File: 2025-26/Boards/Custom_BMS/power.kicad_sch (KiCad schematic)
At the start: 0 parts

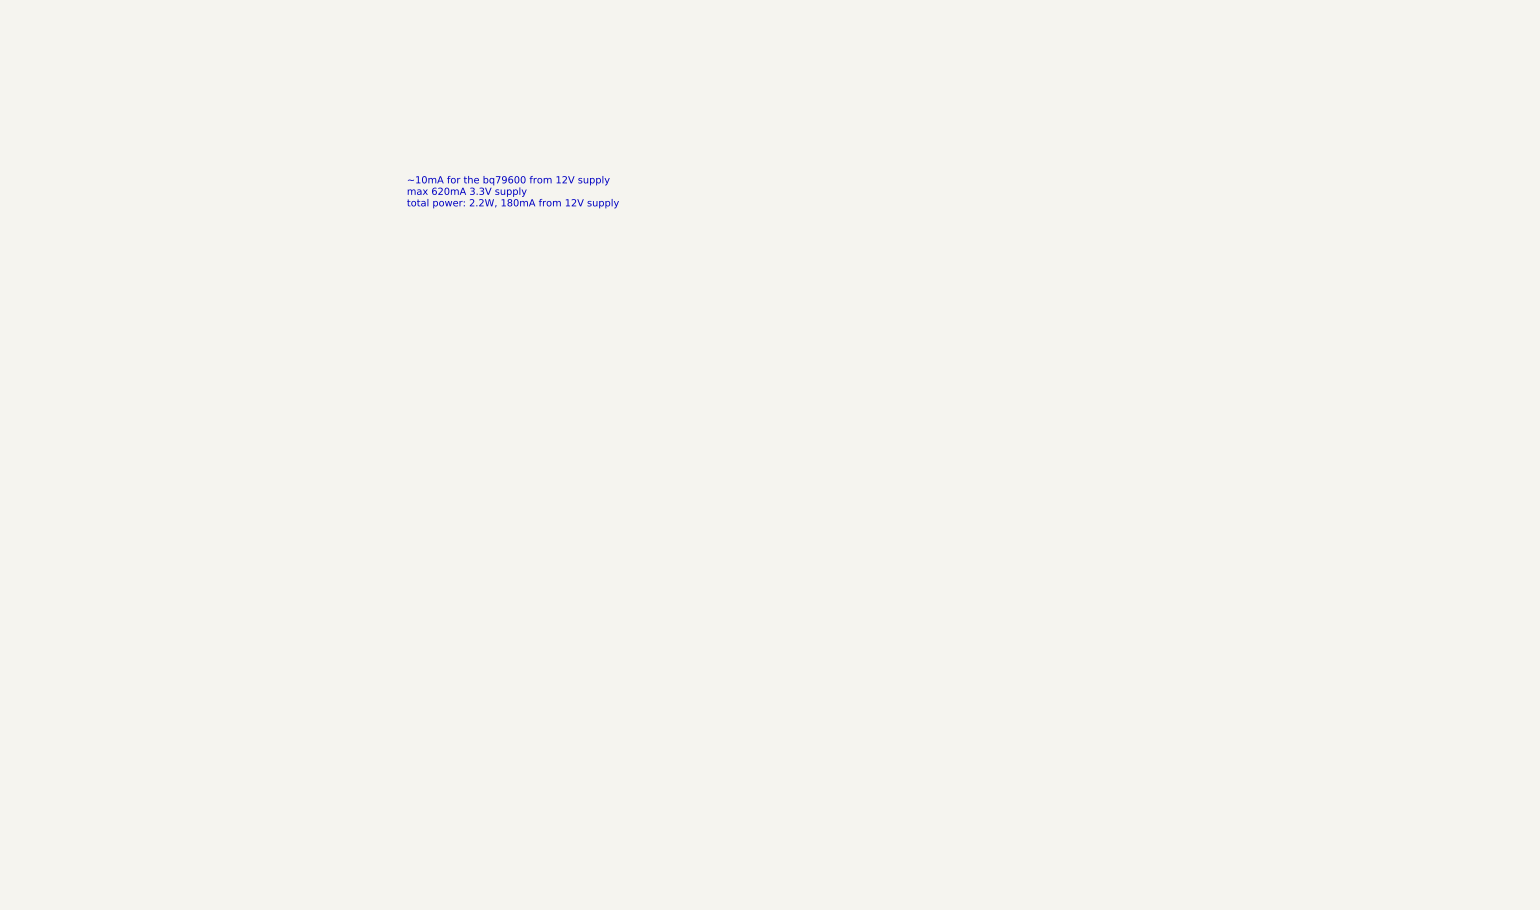
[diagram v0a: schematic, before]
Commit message: designed power circuitry
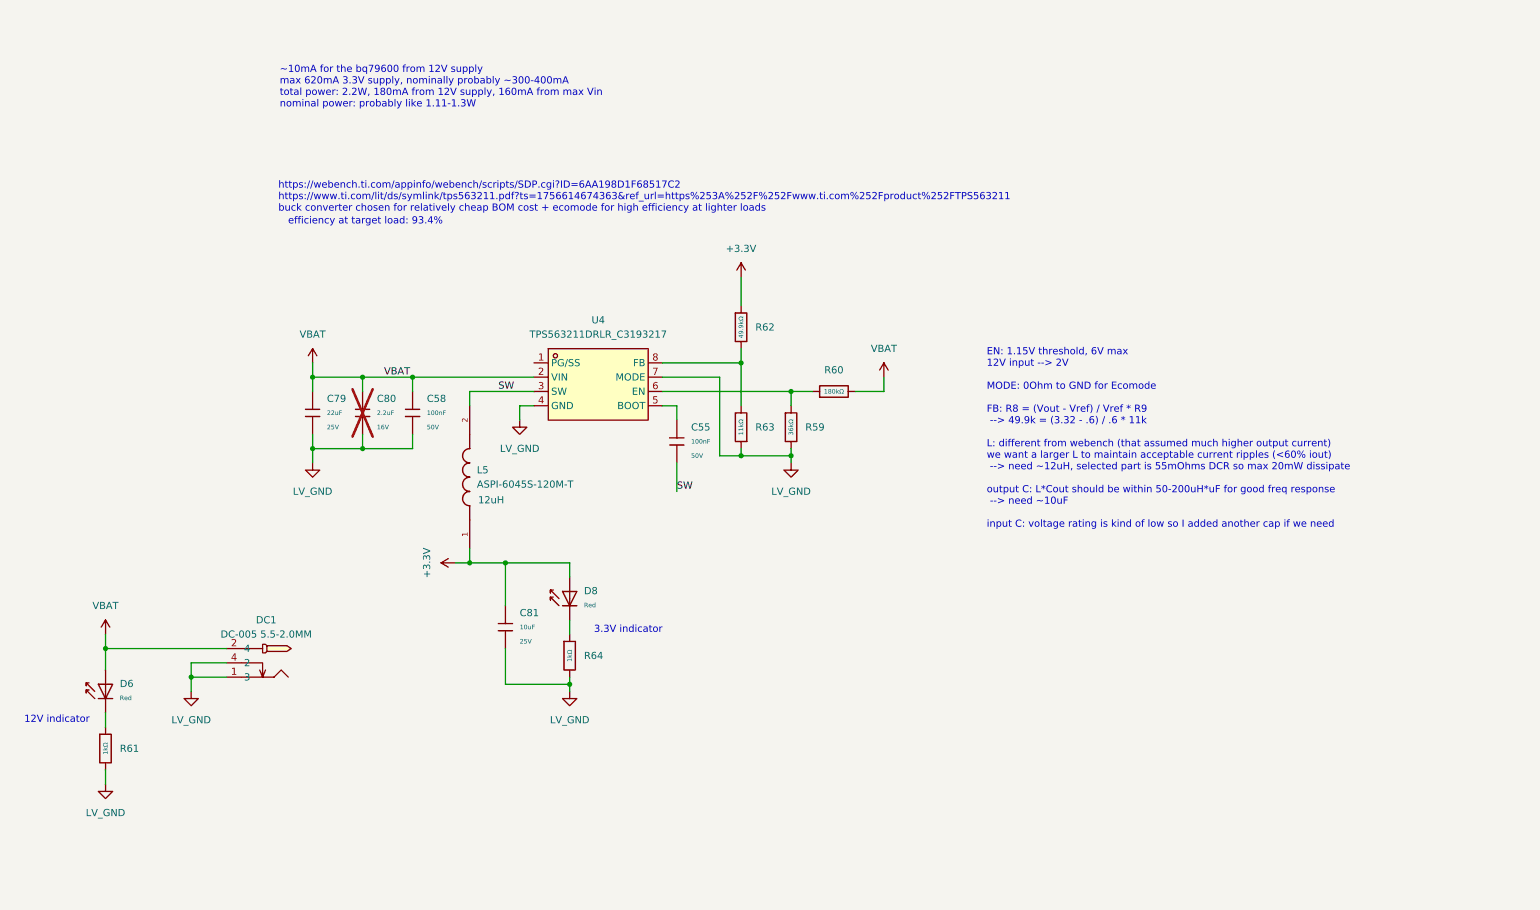
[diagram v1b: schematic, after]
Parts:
- added C55, C58: 100nF, PCM_JLCPCB:C_0603, symbol PCM_JLCPCB-Capacitors:0603,100nF
- added C79: 22uF, PCM_JLCPCB:C_0805, symbol PCM_JLCPCB-Capacitors:0805,22uF
- added C80: 2.2uF, PCM_JLCPCB:C_0603, symbol PCM_JLCPCB-Capacitors:0603,2.2uF
- added C81: 10uF, PCM_JLCPCB:C_0805, symbol PCM_JLCPCB-Capacitors:0805,10uF
- added D6, D8: Red, PCM_JLCPCB:D_0603, symbol PCM_JLCPCB-Diodes:LED,0603,Red
- added DC1: DC-005 5.5-2.0MM, easyeda2kicad:DC-IN-TH_DC-005-5.5-2.0, symbol easyeda2kicad:DC-0055.5-2.0MM
- added L5: ASPI-6045S-120M-T, ASPI-6045S-120M-T:IND_ASPI-6045S-120M-T, symbol ASPI-6045S-120M-T:ASPI-6045S-120M-T
- added R59: 36kΩ, PCM_JLCPCB:R_0603, symbol PCM_JLCPCB-Resistors:0603,36kΩ
- added R60: 180kΩ, PCM_JLCPCB:R_0603, symbol PCM_JLCPCB-Resistors:0603,180kΩ
- added R61, R64: 1kΩ, PCM_JLCPCB:R_0603, symbol PCM_JLCPCB-Resistors:0603,1kΩ
- added R62: 49.9kΩ, PCM_JLCPCB:R_0603, symbol PCM_JLCPCB-Resistors:0603,49.9kΩ
- added R63: 11kΩ, PCM_JLCPCB:R_0603, symbol PCM_JLCPCB-Resistors:0603,11kΩ
- added U4: TPS563211DRLR_C3193217, easyeda2kicad:SOT-583-8_L2.1-W1.6-P0.50-LS1.6-BL, symbol easyeda2kicad:TPS563211DRLR_C3193217
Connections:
- new net: D8.1, R64.1
- new net: C55.1, U4.5 (BOOT)
- new net: D6.1, R61.1
- new net: R59.1, R60.1, U4.6 (EN)
- new net: R62.2, R63.2, U4.8 (FB)
- new net +3.3V: C81.1, D8.2, L5.1, R62.1
- new net LV_GND: C58.2, C79.2, C80.2, C81.2, DC1.1 (3), DC1.4 (2), R59.2, R61.2, R63.1, R64.2, U4.4 (GND), U4.7 (MODE)
- new net SW: C55.2, L5.2, U4.3 (SW)
- new net VBAT: C58.1, C79.1, C80.1, D6.2, DC1.2 (4), R60.2, U4.2 (VIN)
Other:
- note added: "12V indicator"
- note added: "3.3V indicator"
- note added: "EN: 1.15V threshold, 6V maxr 12V input --> 2V MODE: 0Ohm to GND for Ecomode FB: R8 = (Vout - Vref) / Vref * R9 --> 49.9k = (3.32 - .6) / .6 * 11k L: different from webench (that assumed much higher output current) we want a larger L to maintain acceptable current ripples (<60% iout) --> need ~12uH, selected part is 55mOhms DCR so max 20mW dissipate output C: L*Cout should be within 50-200uH*uF fo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"
- note added: "efficiency at target load: 93.4%"
- note added: "https://webench.ti.com/appinfo/webench/scripts/SDP.cgi?ID=6AA198D1F68517C2 https://www.ti.com/lit/ds/symlink/tps563211.pdf?ts=1756614674363&ref_url=https%253A%252F%252Fwww.ti.com%252Fproduct%252FTPS563211 buck converter chosen for relatively cheap BOM cost + ecomode for high efficiency at lighter loads"
- note added: "~10mA for the bq79600 from 12V supply max 620mA 3.3V supply, nominally probably ~300-400mA total power: 2.2W, 180mA from 12V supply, 160mA from max Vin nominal power: probably like 1.11-1.3W"
- note removed: "~10mA for the bq79600 from 12V supply max 620mA 3.3V supply total power: 2.2W, 180mA from 12V supply"

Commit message: reviewed and modified power
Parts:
- removed C81: 10uF, PCM_JLCPCB:C_0805, symbol PCM_JLCPCB-Capacitors:0805,10uF
- removed L5: ASPI-6045S-120M-T, ASPI-6045S-120M-T:IND_ASPI-6045S-120M-T, symbol ASPI-6045S-120M-T:ASPI-6045S-120M-T
- added C10: 4.7uF, PCM_JLCPCB:C_0603, symbol PCM_JLCPCB-Capacitors:0603,4.7uF
- added C9: 10uF, PCM_JLCPCB:C_0603, symbol PCM_JLCPCB-Capacitors:0603,10uF,(2)
- added L5: SRR1206-120ML, IND_BOURNS_SRR1240, symbol SRR1206-120ML:SRR1206-120ML
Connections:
- net +3.3V: now also C10.1, C9.1, L5.2
- net LV_GND: now also C10.2, C9.2
- net SW: now also L5.1
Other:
- note added: "efficiency at target load: 92% thermals: 3.3*~.5*.08*70C/W = ~8C rise"
- note added: "slight correction to the above justification- current ripple is not the best way to calculate it since the buck converter automatically switches to DCM. We still care about voltage ripple though. Below is the current ripple calculation based on voltage ripple, and subsequent inductance. Based on 10mV Vripple and 22uF cap. However, I did not use 22uF (went smaller) since the LC product goes a litt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"
- note removed: "efficiency at target load: 93.4%"
- moved on the sheet: C55, C58, C79, C80, D6, D8, DC1, R59, R60, R61, R62, R63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

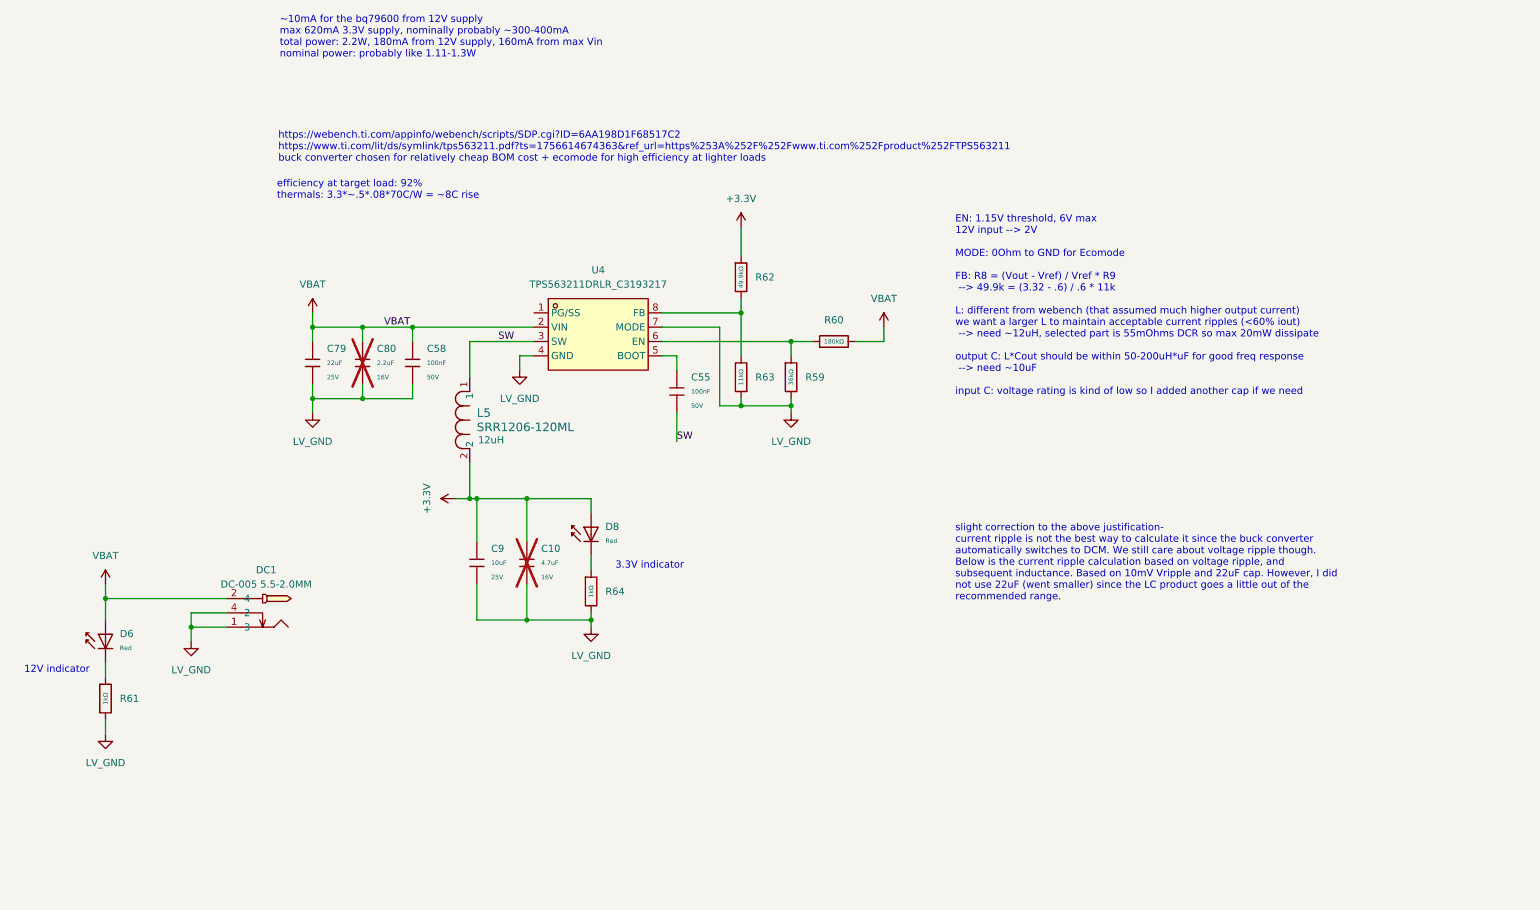
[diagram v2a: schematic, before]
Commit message: added CAN, UART
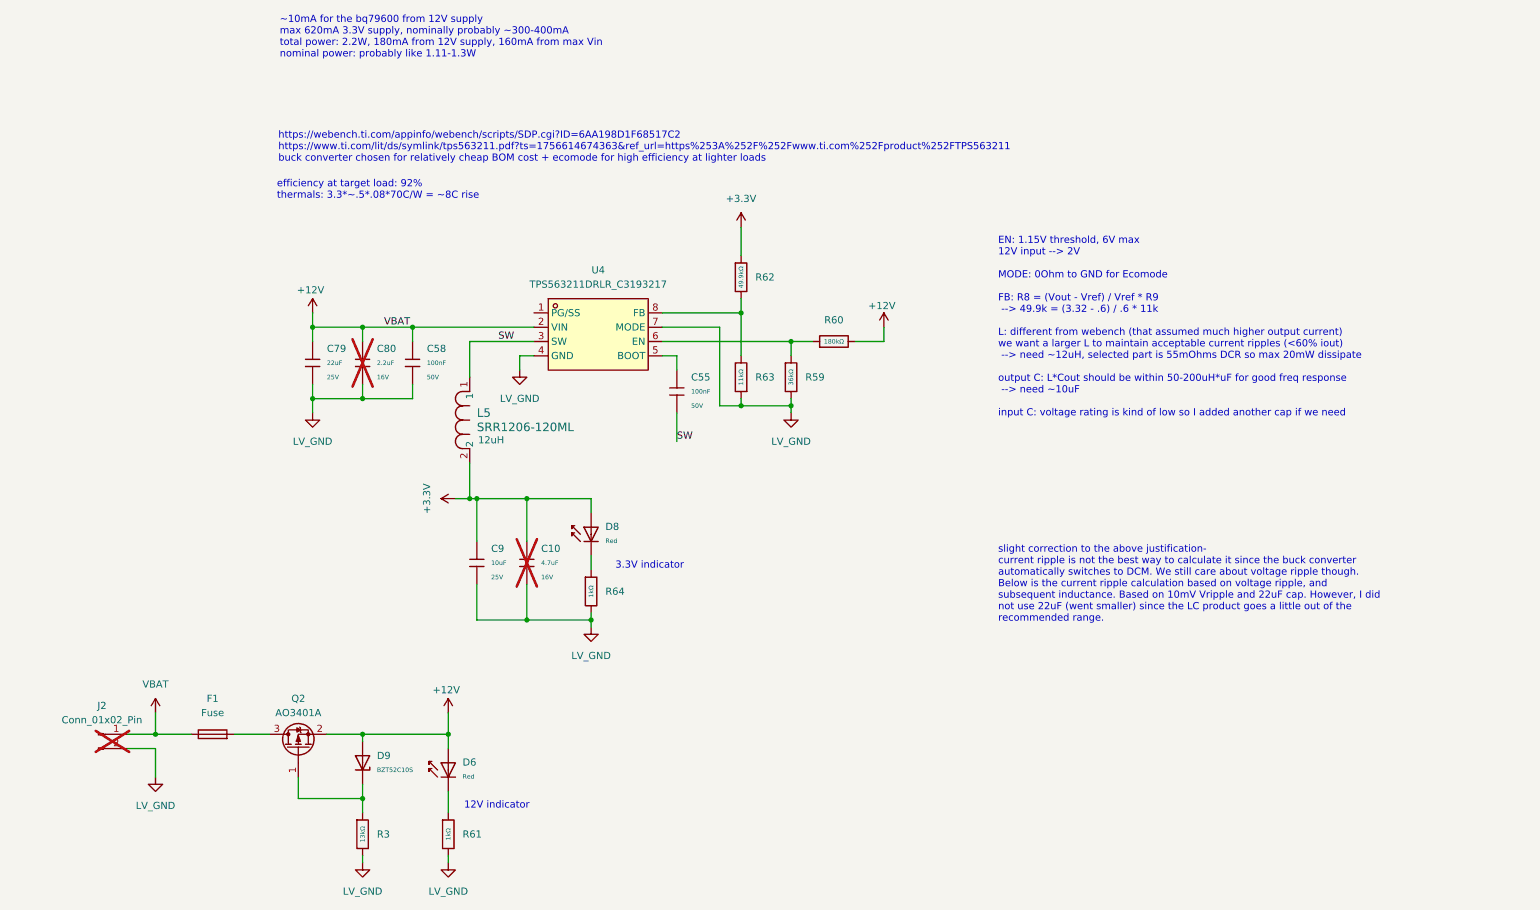
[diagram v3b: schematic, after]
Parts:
- removed DC1: DC-005 5.5-2.0MM, easyeda2kicad:DC-IN-TH_DC-005-5.5-2.0, symbol easyeda2kicad:DC-0055.5-2.0MM
- added D9: BZT52C10S, PCM_JLCPCB:D_SOD-323, symbol PCM_JLCPCB-Diodes:Zener,BZT52C10S
- added F1: Fuse, symbol Device:Fuse
- added J2: Conn_01x02_Pin, symbol Connector:Conn_01x02_Pin
- added Q2: AO3401A, Package_TO_SOT_SMD:SOT-23, symbol Transistor_FET:AO3401A
- added R3: 13kΩ, PCM_JLCPCB:R_0603, symbol PCM_JLCPCB-Resistors:0603,13kΩ
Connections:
- net LV_GND: now also J2.2 (Pin_2), R3.2
- net VBAT renamed +12V
- net +12V: now also D9.2, F1.1, J2.1 (Pin_1), Q2.2 (S)
- new net: D9.1, Q2.1 (G), R3.1
- new net: F1.2, Q2.3 (D)
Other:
- moved on the sheet: D6, R61

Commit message: started layout
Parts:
- removed C10: 4.7uF, PCM_JLCPCB:C_0603, symbol PCM_JLCPCB-Capacitors:0603,4.7uF
- removed C55: 100nF, PCM_JLCPCB:C_0603, symbol PCM_JLCPCB-Capacitors:0603,100nF
- removed C79: 22uF, PCM_JLCPCB:C_0805, symbol PCM_JLCPCB-Capacitors:0805,22uF
- removed C80: 2.2uF, PCM_JLCPCB:C_0603, symbol PCM_JLCPCB-Capacitors:0603,2.2uF
- removed C9: 10uF, PCM_JLCPCB:C_0603, symbol PCM_JLCPCB-Capacitors:0603,10uF,(2)
- removed D8: Red, PCM_JLCPCB:D_0603, symbol PCM_JLCPCB-Diodes:LED,0603,Red
- removed R59: 36kΩ, PCM_JLCPCB:R_0603, symbol PCM_JLCPCB-Resistors:0603,36kΩ
- removed R60: 180kΩ, PCM_JLCPCB:R_0603, symbol PCM_JLCPCB-Resistors:0603,180kΩ
- removed R61, R64: 1kΩ, PCM_JLCPCB:R_0603, symbol PCM_JLCPCB-Resistors:0603,1kΩ
- removed R62: 49.9kΩ, PCM_JLCPCB:R_0603, symbol PCM_JLCPCB-Resistors:0603,49.9kΩ
- removed R63: 11kΩ, PCM_JLCPCB:R_0603, symbol PCM_JLCPCB-Resistors:0603,11kΩ
- removed U4: TPS563211DRLR_C3193217, easyeda2kicad:SOT-583-8_L2.1-W1.6-P0.50-LS1.6-BL, symbol easyeda2kicad:TPS563211DRLR_C3193217
- added C10, C55, C67: 10uF, PCM_JLCPCB:C_0603, symbol PCM_JLCPCB-Capacitors:0603,10uF,(2)
- added C3: 100nF, PCM_JLCPCB:C_0402, symbol PCM_JLCPCB-Capacitors:0402,100nF
- added C68: 100nF, PCM_JLCPCB:C_0603, symbol PCM_JLCPCB-Capacitors:0603,100nF
- added C69: 22uF, PCM_JLCPCB:C_0805, symbol PCM_JLCPCB-Capacitors:0805,22uF
- added D8: Yellow, PCM_JLCPCB:D_0603, symbol PCM_JLCPCB-Diodes:LED,0603,Yellow
- added R19: 13kΩ, PCM_JLCPCB:R_0603, symbol PCM_JLCPCB-Resistors:0603,13kΩ
- added R21: 9.1kΩ, PCM_JLCPCB:R_0603, symbol PCM_JLCPCB-Resistors:0603,9.1kΩ
- added R34: 47kΩ, PCM_JLCPCB:R_0402, symbol PCM_JLCPCB-Resistors:0402,47kΩ
- added R59: 2.2kΩ, PCM_JLCPCB:R_0402, symbol PCM_JLCPCB-Resistors:0402,2.2kΩ
- added R60: 10kΩ, PCM_JLCPCB:R_0402, symbol PCM_JLCPCB-Resistors:0402,10kΩ
- added R61: 3kΩ, PCM_JLCPCB:R_0603, symbol PCM_JLCPCB-Resistors:0603,3kΩ
- added U2: TPS563300, Package_TO_SOT_SMD:SOT-583-8, symbol Regulator_Switching:TPS563300
- added U4: AMS1117-3.3, Package_TO_SOT_SMD:SOT-223-3_TabPin2, symbol Regulator_Linear:AMS1117-3.3
- F1: footprint (none) -> Fuse:Fuse_0603_1608Metric_Pad1.05x0.95mm_HandSolder
- J2: footprint (none) -> Connector_PinHeader_2.00mm:PinHeader_1x02_P2.00mm_Vertical
- L5: Inductance 12uH -> (none)
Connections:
- net +12V: now also D9.1, C10.1, R60.1, U2.3 (VIN); no longer D9.2, F1.1, J2.1 (Pin_1)
- net +3.3V: now also C69.1, D8.2, U4.2 (VO); no longer L5.2
- net LV_GND: now also C10.2, C55.2, C67.2, C68.2, C69.2, R19.2, R21.2, R59.2, R61.2, U2.4 (GND), U4.1 (GND)
- net at Q2.1 (G), R3.1: now also D9.2; no longer D9.1
- net at D6.1: now also R19.1
- net SW renamed +5V
- net +5V: now also C55.1, C67.1, C68.1, R34.1, U4.3 (VI)
- new net: D8.1, R61.1
- new net: C3.2, L5.2, U2.5 (SW)
- new net: R21.1, R34.2, U2.8 (FB)
- new net: R59.1, R60.2, U2.2 (EN)
- new net: C3.1, U2.6 (BST)
- new net VBAT: F1.1, J2.1 (Pin_1)
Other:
- note added: "1.1-1.3V dropout even at worse input voltage ripple (4.7V), still clears the dropout thermal resistance to ambient not provided (junction to case provided though, that's 15 C/W) but max would be .5W so I'm thinking that'll be fine if the layout is good"
- note added: "EN: 1.15V threshold, 6V maxr 12V input --> 2V FB: R8 = (Vout - Vref) / Vref * R9 --> 47k = (5 - .8) / .8 * 9k L: following the equation would suggest you need a 62uH inductor to maintain a reasonable current ripple. However since the converter goes into DCM automatically, we can simply choose any inductor and make sure the inductor can handle the peak current without saturating. Ipk = Vin * D / (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"
- note added: "OC/RP protection circuit"
- note added: "efficiency at target load: 93% thermals: 5*~.2*.07*60.2C/W = ~4.2C rise"
- note added: "~10mA for the bq79600 from 12V supply max 240mA 3.3V supply, although there's another thing in the datasheet that says max power for the selected package is 435mW max power: <1W, 76mA from 12V supply, 65mA from max Vin"
- note removed: "EN: 1.15V threshold, 6V maxr 12V input --> 2V MODE: 0Ohm to GND for Ecomode FB: R8 = (Vout - Vref) / Vref * R9 --> 49.9k = (3.32 - .6) / .6 * 11k L: different from webench (that assumed much higher output current) we want a larger L to maintain acceptable current ripples (<60% iout) --> need ~12uH, selected part is 55mOhms DCR so max 20mW dissipate output C: L*Cout should be within 50-200uH*uF fo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"
- note removed: "efficiency at target load: 92% thermals: 3.3*~.5*.08*70C/W = ~8C rise"
- note removed: "https://webench.ti.com/appinfo/webench/scripts/SDP.cgi?ID=6AA198D1F68517C2 https://www.ti.com/lit/ds/symlink/tps563211.pdf?ts=1756614674363&ref_url=https%253A%252F%252Fwww.ti.com%252Fproduct%252FTPS563211 buck converter chosen for relatively cheap BOM cost + ecomode for high efficiency at lighter loads"
- note removed: "slight correction to the above justification- current ripple is not the best way to calculate it since the buck converter automatically switches to DCM. We still care about voltage ripple though. Below is the current ripple calculation based on voltage ripple, and subsequent inductance. Based on 10mV Vripple and 22uF cap. However, I did not use 22uF (went smaller) since the LC product goes a litt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"
- note removed: "~10mA for the bq79600 from 12V supply max 620mA 3.3V supply, nominally probably ~300-400mA total power: 2.2W, 180mA from 12V supply, 160mA from max Vin nominal power: probably like 1.11-1.3W"
- moved on the sheet: C58, D6, D9, F1, J2, Q2, R3
